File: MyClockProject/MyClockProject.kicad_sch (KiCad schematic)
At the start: 22 parts, among them J1 Conn_01x16_Socket_ESP32, J2 Conn_01x16_Socket_ESP32, J3 USB_C_Receptacle_PowerOnly_6P, J4 RJ45, J5 Conn_01x05_Socket, J6 Conn_01x05_Pin, J7 Barrel_Jack, J8 Conn_01x03_Socket, J9 Conn_01x03_Pin, U1 ULN2003A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

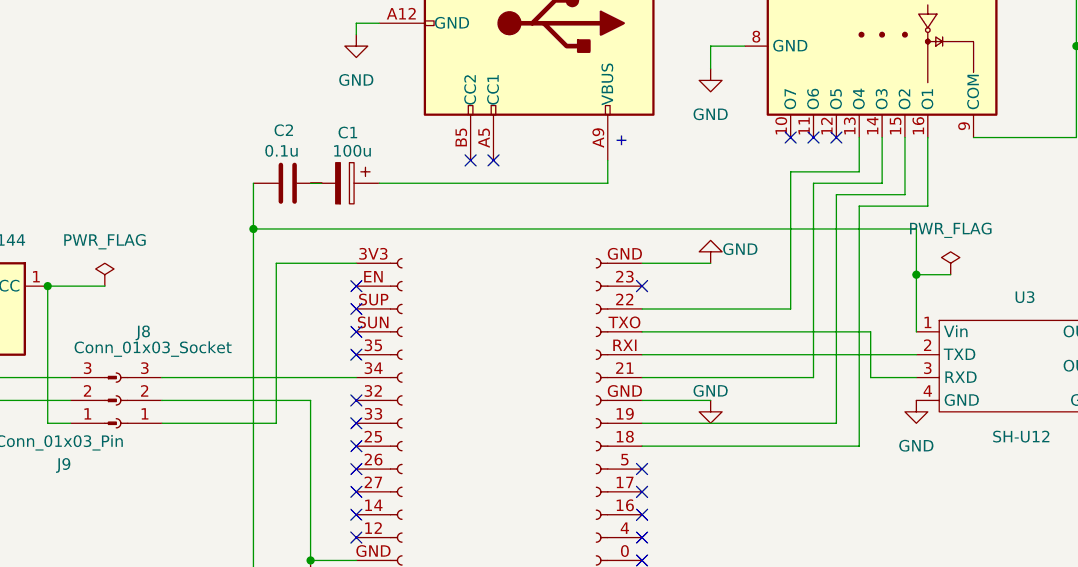
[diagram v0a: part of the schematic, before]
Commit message: 基盤を完成しました。５Vからのコンデンサの配線を修正しました。ホールセンサーを接続できるようにしました。
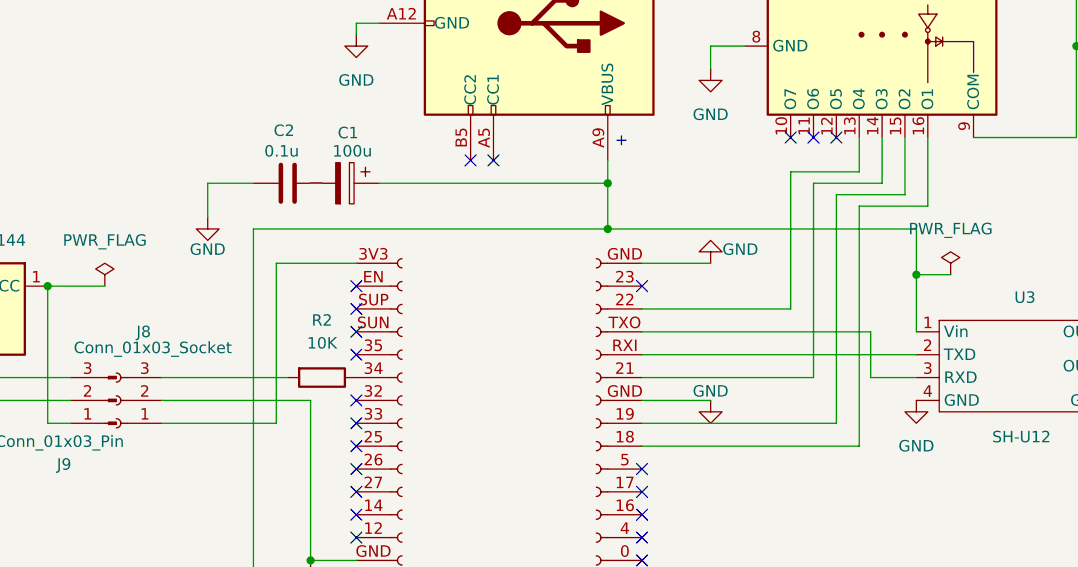
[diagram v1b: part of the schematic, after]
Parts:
- added R2: 10K, Resistor_THT:R_Axial_DIN0309_L9.0mm_D3.2mm_P2.54mm_Vertical, symbol Device:R
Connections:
- net GND: now also C2.2
- net at J1.５V (Pin_16), U3.1 (Vin): now also C1.1, J3.A9 (VBUS), J3.B9 (VBUS); no longer C2.2
- net at J1.34 (Pin_6): now also R2.1; no longer J8.3 (Pin_3)
- new net: J8.3 (Pin_3), R2.2
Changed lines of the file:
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@@
 	)
 	(junction
-		(at 83.82 96.52)
+		(at 167.64 53.34)
 		(diameter 0)
 		(color 0 0 0 0)
 	)
 	(junction
-		(at 167.64 53.34)
+		(at 157.48 53.34)
 		(diameter 0)
 		(color 0 0 0 0)
 	)
 	(junction
-		(at 157.48 53.34)
+		(at 60.96 102.87)
 		(diameter 0)
 		(color 0 0 0 0)
 	)
 	(junction
-		(at 60.96 102.87)
+		(at 123.19 96.52)
 		(diameter 0)
 		(color 0 0 0 0)
@@
 	)
 	(junction
+		(at 123.19 91.44)
+		(diameter 0)
+		(color 0 0 0 0)
+	)
+	(junction
 		(at 187.96 91.44)
 		(diameter 0)
@@
 	(wire
 		(pts
+			(xy 83.82 91.44) (xy 78.74 91.44)
+		)
+		(stroke
+			(width 0)
+			(type default)
+		)
+	)
+	(wire
+		(pts
 			(xy 187.96 88.9) (xy 187.96 91.44)
 		)
@@
 	(wire
 		(pts
+			(xy 73.66 113.03) (xy 87.63 113.03)
+		)
+		(stroke
+			(width 0)
+			(type default)
+		)
+	)
+	(wire
+		(pts
 			(xy 185.42 107.95) (xy 185.42 114.3)
 		)
@@
 	(wire
 		(pts
-			(xy 73.66 113.03) (xy 95.25 113.03)
-		)
-		(stroke
-			(width 0)
-			(type default)
-		)
-	)
-	(wire
-		(pts
 			(xy 152.4 113.03) (xy 157.48 113.03)
 		)
@@
 	(wire
 		(pts
+			(xy 123.19 91.44) (xy 123.19 96.52)
+		)
+		(stroke
+			(width 0)
+			(type default)
+		)
+	)
+	(wire
+		(pts
 			(xy 86.36 100.33) (xy 95.25 100.33)
 		)
@@
 	(wire
 		(pts
-			(xy 83.82 96.52) (xy 157.48 96.52)
+			(xy 83.82 96.52) (xy 123.19 96.52)
 		)
 		(stroke
@@
 	(wire
 		(pts
+			(xy 123.19 96.52) (xy 157.48 96.52)
+		)
+		(stroke
+			(width 0)
+			(type default)
+		)
+	)
+	(wire
+		(pts
 			(xy 134.62 76.2) (xy 134.62 78.74)
 		)
@@
 	(wire
 		(pts
-			(xy 153.67 91.44) (xy 153.67 86.36)
+			(xy 78.74 91.44) (xy 78.74 95.25)
 		)
 		(stroke
@@
 	(wire
 		(pts
-			(xy 175.26 45.72) (xy 175.26 76.2)
+			(xy 153.67 91.44) (xy 153.67 86.36)
 		)
 		(stroke
@@
 	(wire
 		(pts
-			(xy 198.12 114.3) (xy 191.77 114.3)
+			(xy 175.26 45.72) (xy 175.26 76.2)
 		)
 		(stroke
@@
 	(wire
 		(pts
-			(xy 83.82 96.52) (xy 83.82 138.43)
+			(xy 198.12 114.3) (xy 191.77 114.3)
 		)
 		(stroke
@@
 	(wire
 		(pts
-			(xy 185.42 71.12) (xy 181.61 71.12)
+			(xy 83.82 96.52) (xy 83.82 138.43)
 		)
 		(stroke
@@
 	(wire
 		(pts
-			(xy 198.12 109.22) (xy 198.12 114.3)
+			(xy 185.42 71.12) (xy 181.61 71.12)
 		)
 		(stroke
@@
 	(wire
 		(pts
-			(xy 181.61 76.2) (xy 185.42 76.2)
+			(xy 198.12 109.22) (xy 198.12 114.3)
 		)
 		(stroke
@@
 	(wire
 		(pts
-			(xy 83.82 91.44) (xy 83.82 96.52)
+			(xy 181.61 76.2) (xy 185.42 76.2)
 		)
 		(stroke
@@
 	(symbol
 		(lib_id "power:GND")
+		(at 78.74 95.25 0)
+		(unit 1)
+		(body_style 1)
+		(exclude_from_sim no)
+		(in_bom yes)
+		(on_board yes)
+		(in_pos_files yes)
+		(dnp no)
+		(property "Reference" "#PWR012"
+			(at 78.74 101.6 0)
+			(hide yes)
+			(show_name no)
+			(do_not_autoplace no)
+			(effects
+				(font
+					(size 1.27 1.27)
+				)
+			)
+		)
+		(property "Value" "GND"
+			(at 78.74 98.806 0)
+			(show_name no)
+			(do_not_autoplace no)
+			(effects
+				(font
+					(size 1.27 1.27)
+				)
+			)
+		)
+		(property "Footprint" ""
+			(at 78.74 95.25 0)
+			(hide yes)
+			(show_name no)
+			(do_not_autoplace no)
+			(effects
+				(font
+					(size 1.27 1.27)
+				)
+			)
+		)
+		(property "Datasheet" ""
+			(at 78.74 95.25 0)
+			(hide yes)
+			(show_name no)
+			(do_not_autoplace no)
+			(effects
+				(font
+					(size 1.27 1.27)
+				)
+			)
+		)
+		(property "Description" "Power symbol creates a global label with name \"GND\" , ground"
+			(at 78.74 95.25 0)
+			(hide yes)
+			(show_name no)
+			(do_not_autoplace no)
+			(effects
+				(font
+					(size 1.27 1.27)
+				)
+			)
+		)
+		(pin "1"
+		)
+		(instances
+			(project "MyClockProject"
+				(path "/6175afd2-2183-4758-9b67-a4adfb76e371"
+					(reference "#PWR012")
+					(unit 1)
+				)
+			)
+		)
+	)
+	(symbol
+		(lib_id "power:GND")
 		(at 167.64 55.88 0)
 		(unit 1)
@@
 					(unit 1)
 				)
+			)
+		)
+	)
+	(symbol
+		(lib_id "Device:R")
+		(at 91.44 113.03 270)
+		(unit 1)
+		(body_style 1)
+		(exclude_from_sim no)
+		(in_bom yes)
+		(on_board yes)
+		(in_pos_files yes)
+		(dnp no)
+		(fields_autoplaced yes)
+		(property "Reference" "R2"
+			(at 91.44 106.68 90)
+			(show_name no)
+			(do_not_autoplace no)
+			(effects
+				(font
+					(size 1.27 1.27)
+				)
+			)
+		)
+		(property "Value" "10K"
+			(at 91.44 109.22 90)
+			(show_name no)
+			(do_not_autoplace no)
+			(effects
+				(font
+					(size 1.27 1.27)
+				)
+			)
+		)
+		(property "Footprint" "Resistor_THT:R_Axial_DIN0309_L9.0mm_D3.2mm_P2.54mm_Vertical"
+			(at 91.44 111.252 90)
+			(hide yes)
+			(show_name no)
+			(do_not_autoplace no)
+			(effects
+				(font
+					(size 1.27 1.27)
+				)
+			)
+		)
+		(property "Datasheet" ""
+			(at 91.44 113.03 0)
+			(hide yes)
+			(show_name no)
+			(do_not_autoplace no)
+			(effects
+				(font
+					(size 1.27 1.27)
+				)
+			)
+		)
+		(property "Description" "Resistor"
+			(at 91.44 113.03 0)
+			(hide yes)
+			(show_name no)
+			(do_not_autoplace no)
+			(effects
+				(font
+					(size 1.27 1.27)
+				)
+			)
+		)
+		(pin "1"
+		)
+		(pin "2"
+		)
+		(instances
+			(project "MyClockProject"
+				(path "/6175afd2-2183-4758-9b67-a4adfb76e371"
+					(reference "R2")
+					(unit 1)
+				)
